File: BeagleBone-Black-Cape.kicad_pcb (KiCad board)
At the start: 2 copper layers, 54.6 x 86.9 mm, 48 parts, among them J1 MC000052, J10 MOLEX_2031, J11 MOLEX_2021, J12 EBV-02-D, J2 MOLEX_2051, J3 MOLEX_2031, J4 MOLEX_2021, J5 MOLEX_2041, J6 MOLEX_2031, J7 MOLEX_2041, J8 MOLEX_2031, J9 MOLEX_2041, P1 BeagleBone_Black_Header, P2 BeagleBone_Black_Header, Q1 IRLB8721PBF, Q2 IRFML8244, U1 DIGIPOT_50K, U2 U_IC-HKB, U3 X_STEPPER, U4 Y_STEPPER, U5 Z_STEPPER

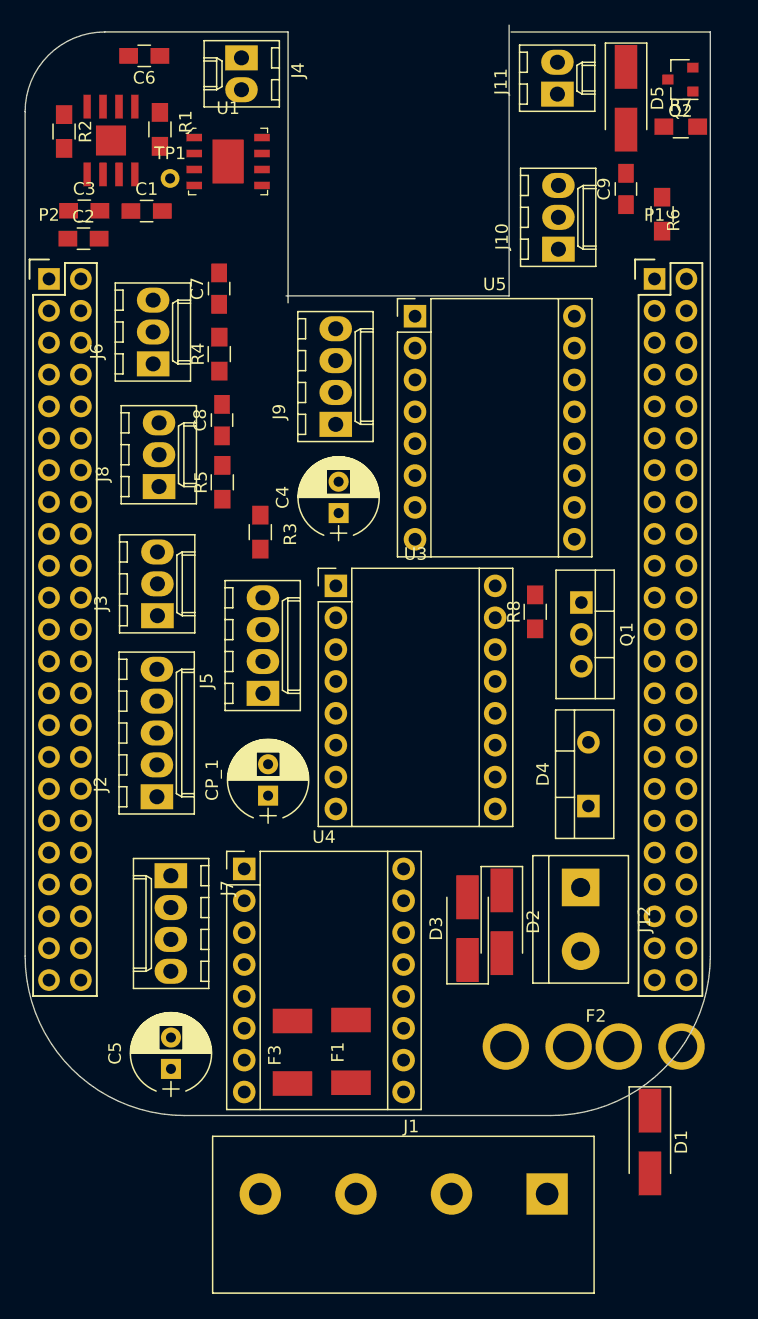
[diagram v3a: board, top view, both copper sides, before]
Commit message: moved power connector into direction of ethernet port idea is that board is placed on male headers to create more space
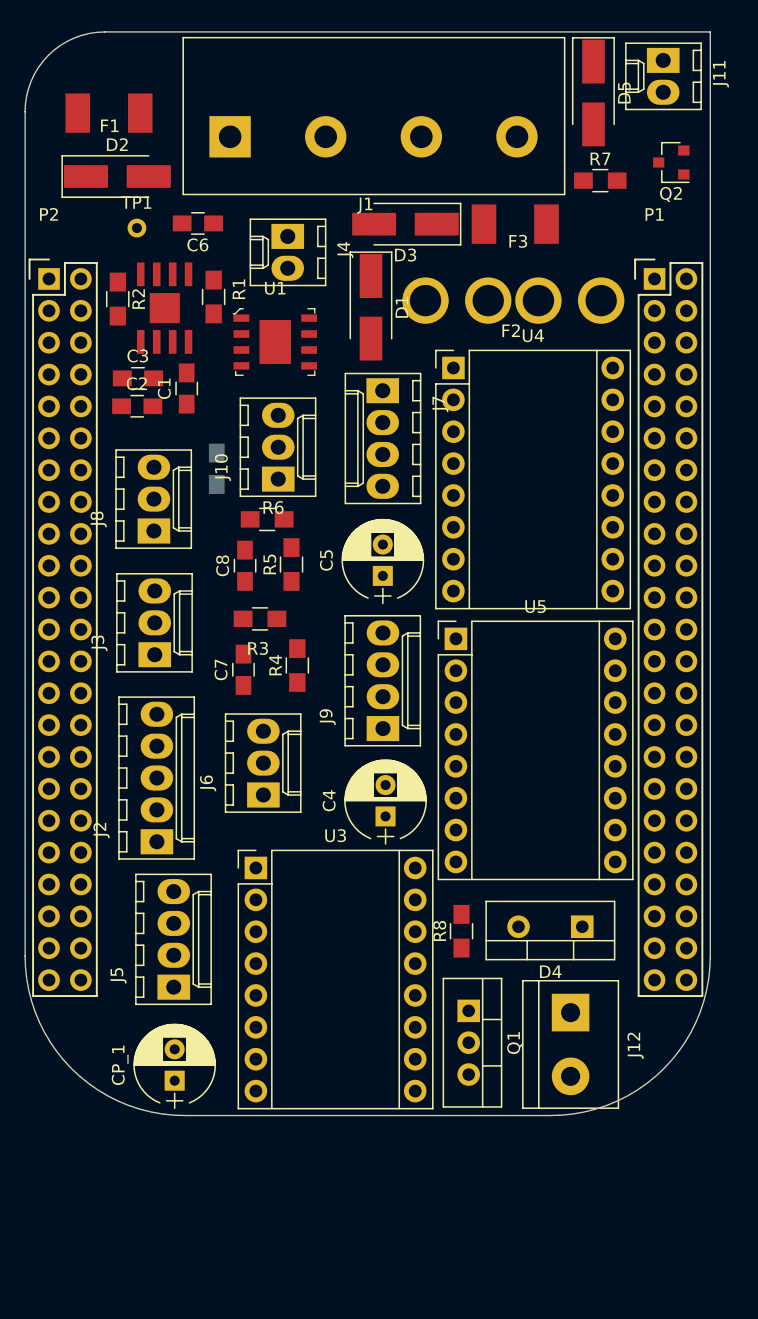
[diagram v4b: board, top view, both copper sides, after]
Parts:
- C9: moved to B.Cu
- moved J1 86.7 mm to (153.7, 51.1), turned to 180 degrees
- moved F1 77.3 mm to (121.2, 49.2), turned to 0 degrees
- moved D1 70.1 mm to (142.0, 64.6)
- moved F3 68.4 mm to (153.6, 58.0), turned to 0 degrees
- moved D2 66.8 mm to (121.8, 54.2), turned to 0 degrees
- moved F2 59.8 mm to (153.4, 64.1), turned to 180 degrees
- moved D3 56.4 mm to (144.8, 58.0), turned to 180 degrees
- moved U4 43.3 mm to (148.6, 69.5)
- moved C5 42.8 mm to (143.0, 86.1)
- moved J7 42.2 mm to (143.0, 71.3)
- moved R6 39.8 mm to (133.8, 81.5), turned to 180 degrees
- moved C9 39.5 mm to (129.7, 77.5), turned to 270 degrees
- moved J6 35.5 mm to (133.5, 103.5)
- moved Q1 33.8 mm to (149.8, 120.7)
- moved C7 30.4 mm to (131.9, 93.5)
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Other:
- board size 54.6 x 86.9 mm -> 54.6 x 86.4 mm

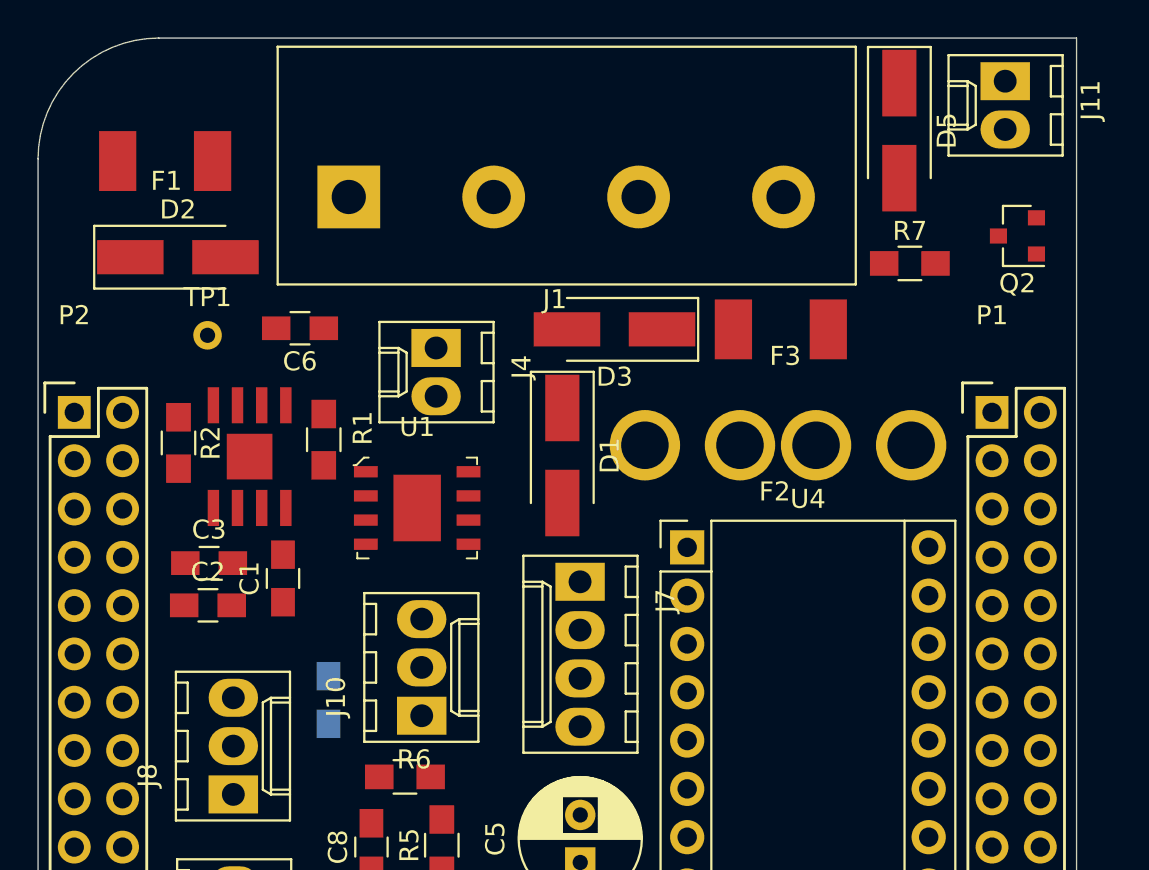
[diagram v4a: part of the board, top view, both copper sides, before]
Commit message: reorganized pcb and updated footprints
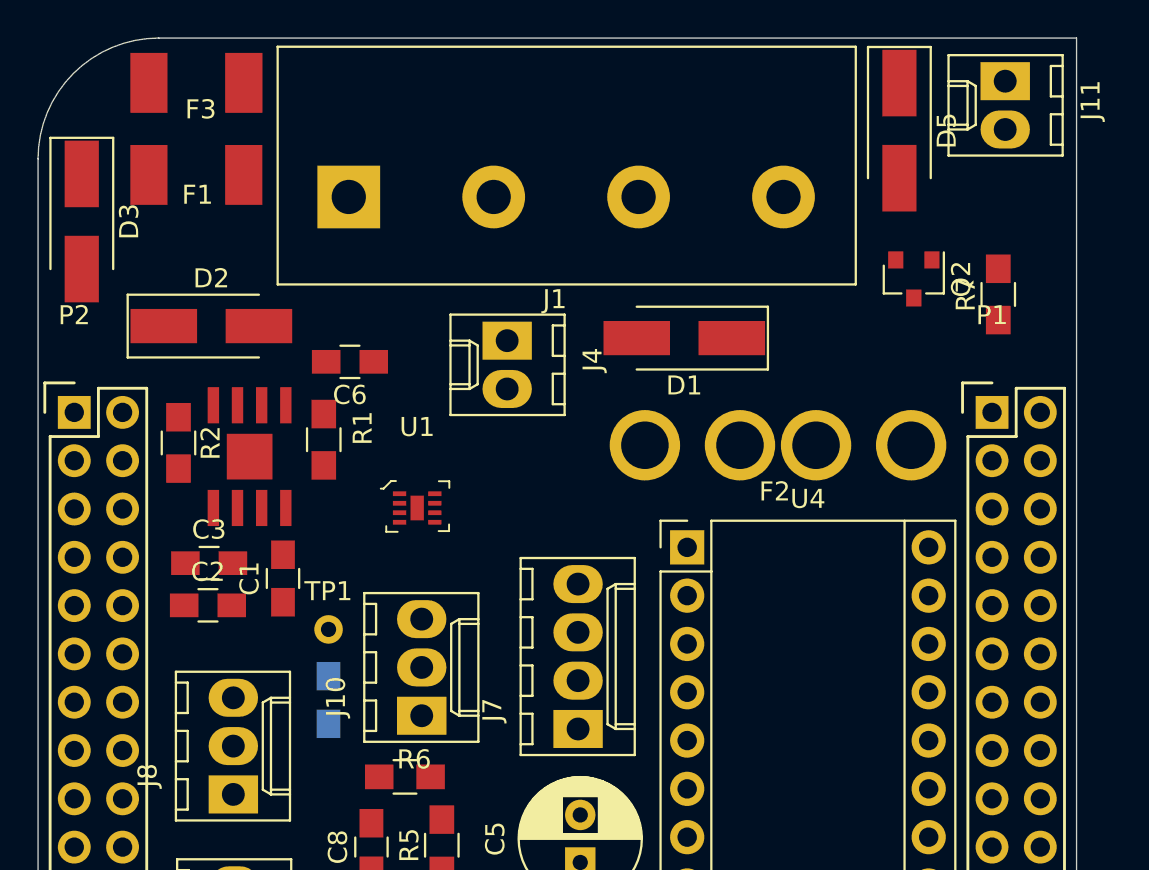
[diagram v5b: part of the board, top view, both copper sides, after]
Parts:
- moved F3 33.4 mm to (122.8, 45.1)
- moved D3 28.6 mm to (116.8, 52.3), turned to 270 degrees
- moved TP1 16.7 mm to (129.7, 73.8)
- moved D1 8.90 mm to (148.4, 58.5), turned to 180 degrees
- moved J7 7.74 mm to (142.9, 79.0), turned to 90 degrees
- moved Q2 5.90 mm to (160.5, 55.4), turned to 270 degrees
- moved R7 4.92 mm to (165.0, 56.2), turned to 90 degrees
- moved D2 4.03 mm to (123.6, 57.8)
- moved J4 3.76 mm to (139.1, 58.6)
- moved C6 3.17 mm to (130.9, 59.7)
- moved F1 1.80 mm to (122.8, 49.9)
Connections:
- D5 pad 1: +12V -> +24V
- J11 pad 1: +12V -> +24V
- J5 pad 1: X_1A -> X_2B
- J5 pad 2: X_1B -> X_2A
- J5 pad 3: X_2A -> X_1A
- J5 pad 4: X_2B -> X_1B
- J7 pad 1: Y_1A -> Y_2B
- J7 pad 2: Y_1B -> Y_2A
- J7 pad 3: Y_2A -> Y_1A
- J7 pad 4: Y_2B -> Y_1B
- J9 pad 1: Z_1A -> Z_2B
- J9 pad 2: Z_1B -> Z_2A
- J9 pad 3: Z_2A -> Z_1A
- J9 pad 4: Z_2B -> Z_1B
- P1 pad 13: SPINDLE_PWM -> FAN_PWM
- P1 pad 19: FAN_PWM -> SPINDLE_PWM

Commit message: started creating tracks
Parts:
- moved D3 5.95 mm to (122.0, 49.5), turned to 0 degrees
- moved R2 5.85 mm to (127.4, 65.8)
- moved U2 5.85 mm to (131.1, 66.6)
- moved R1 5.85 mm to (135.0, 65.7)
- moved U1 5.20 mm to (139.4, 66.0)
- moved F1 3.97 mm to (121.3, 53.6)
- moved C6 2.04 mm to (131.8, 57.9)
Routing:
- net GND: track 0.00 -> 168.2 mm
- net +24V: track 0.00 -> 98.4 mm
- net +12V: track 0.00 -> 37.3 mm
- net FAN_PWM: track 0.00 -> 30.1 mm
- net Net-(F2-Pad1): track 0.00 -> 29.6 mm
- net +5V: track 0.00 -> 26.6 mm
- net Net-(F3-Pad2): track 0.00 -> 23.2 mm
- net Net-(D5-Pad2): track 0.00 -> 12.0 mm
- net Net-(F1-Pad2): track 0.00 -> 8.62 mm

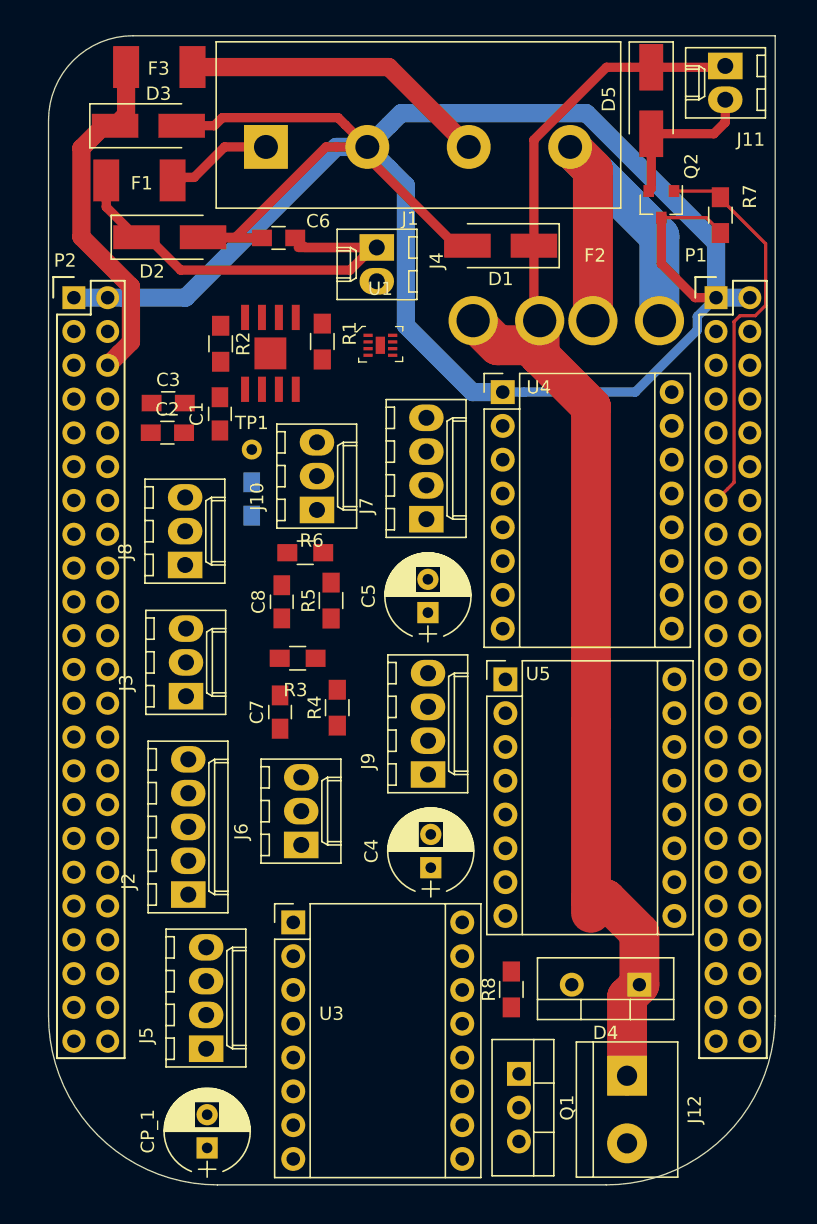
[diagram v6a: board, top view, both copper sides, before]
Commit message: added ground and power plane restored of 0, 5, 12, 24v connectors
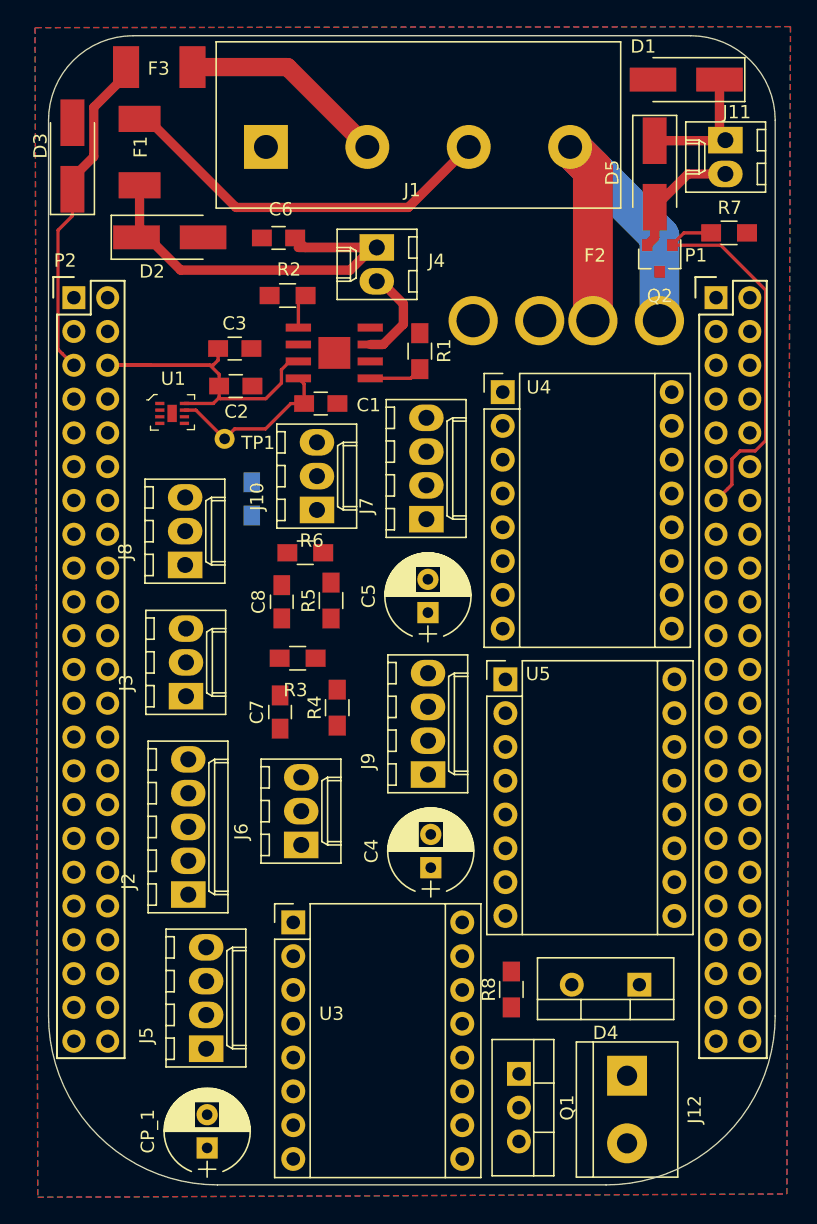
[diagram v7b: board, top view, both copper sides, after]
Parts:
- moved D1 18.7 mm to (162.4, 46.0)
- moved U1 16.5 mm to (123.8, 71.1)
- moved C1 7.62 mm to (134.9, 70.3), turned to 180 degrees
- moved R1 7.37 mm to (142.4, 66.4), turned to 90 degrees
- moved C3 6.46 mm to (128.5, 66.2), turned to 180 degrees
- moved C2 6.22 mm to (128.5, 69.0), turned to 180 degrees
- moved R2 6.20 mm to (132.4, 62.2), turned to 0 degrees
- moved D3 6.14 mm to (116.3, 51.7), turned to 90 degrees
- moved J11 5.58 mm to (165.3, 50.5)
- moved D5 5.53 mm to (160.0, 53.1)
- moved U2 4.80 mm to (135.9, 66.5), turned to 90 degrees
- moved Q2 4.07 mm to (160.4, 59.4)
- moved TP1 2.19 mm to (127.7, 73.0)
- moved F1 2.18 mm to (121.3, 51.4), turned to 90 degrees
- moved R7 1.48 mm to (165.6, 57.5), turned to 180 degrees
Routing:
- net GND: track 168.2 -> 0.57 mm
- net +24V: track 98.4 -> 10.1 mm
- net +5V: track 26.6 -> 58.6 mm
- net Net-(F1-Pad2): track 8.62 -> 29.4 mm
- net POT_W: track 0.00 -> 13.1 mm
- net Net-(F3-Pad2): track 23.2 -> 15.6 mm
- net LDK: track 0.00 -> 7.35 mm
- net IC_HB_PWM1: track 0.00 -> 4.01 mm
- net IC_HB_PWM2: track 0.00 -> 2.63 mm
- net Net-(D5-Pad2): track 12.0 -> 9.44 mm
- net +12V: track 37.3 -> 36.1 mm
- added copper zone on B.Cu, net +24V
- added copper zone on F.Cu, net GND
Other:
- outline, holes or cut-outs redrawn

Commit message: finished routing board....
still need to final check, add some text and make crucial tracks wider
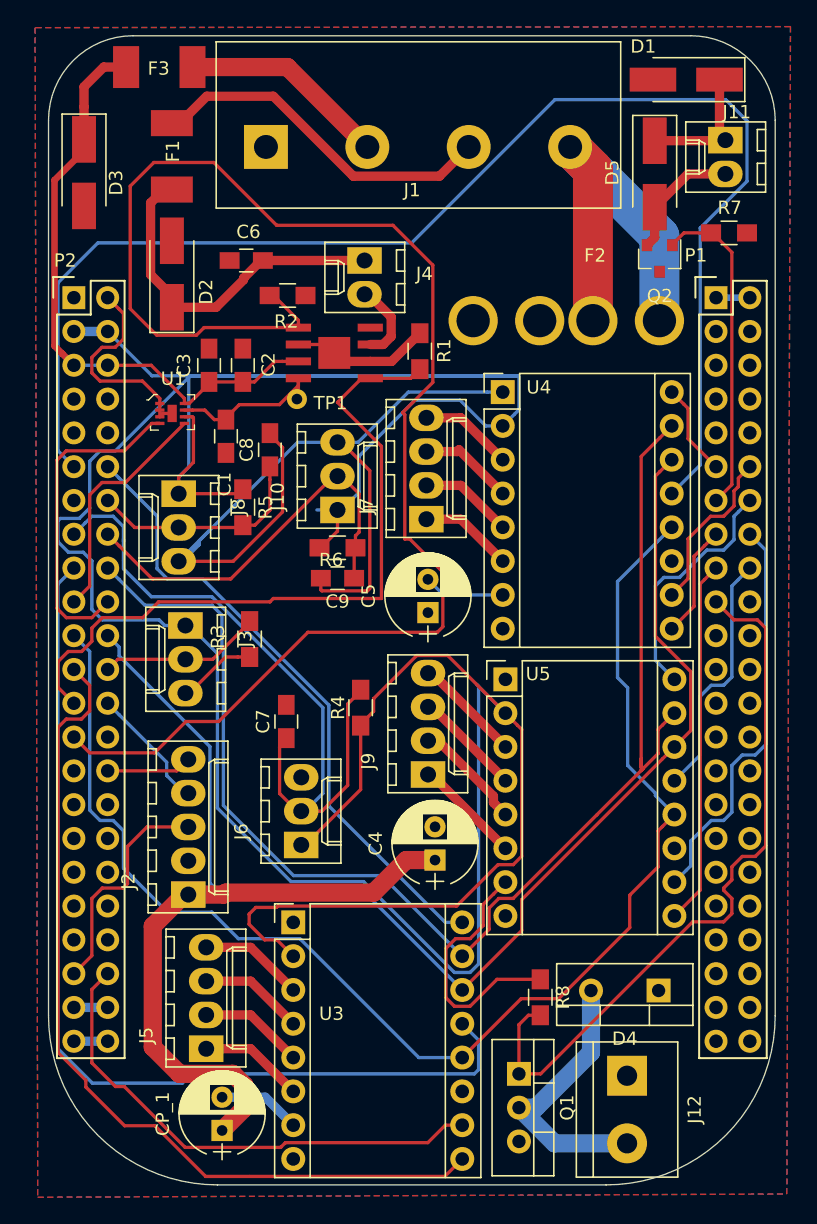
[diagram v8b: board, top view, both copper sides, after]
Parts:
- C9: moved to F.Cu
- moved C8 11.5 mm to (131.1, 73.8)
- moved R5 9.65 mm to (129.1, 78.1), turned to 270 degrees
- moved C9 8.78 mm to (136.2, 83.5), turned to 180 degrees
- moved C1 7.53 mm to (127.8, 72.8), turned to 90 degrees
- moved TP1 6.20 mm to (133.1, 70.0)
- moved J8 5.38 mm to (124.2, 77.1), turned to 270 degrees
- moved J3 5.31 mm to (124.8, 87.0), turned to 270 degrees
- moved R3 3.89 mm to (129.6, 88.0), turned to 90 degrees
- moved C6 2.96 mm to (129.3, 59.6)
- moved D2 2.77 mm to (123.7, 60.6), turned to 90 degrees
- moved R6 2.45 mm to (136.2, 81.2), turned to 0 degrees
- moved F1 2.45 mm to (123.7, 51.7)
- moved C3 2.30 mm to (126.5, 67.5), turned to 270 degrees
- moved R8 2.25 mm to (151.4, 115.0), turned to 270 degrees
- moved R4 1.76 mm to (137.9, 93.2)
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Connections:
- P1 pad 11: Y_DIR -> Y_ENABLE
- P1 pad 15: Z_DIR -> Y_DIR
- P1 pad 17: Y_ENABLE -> Z_DIR
- P1 pad 18: Z_PO -> SPIO_CSZ
- P2 pad 12: X_DIR -> X_ENABLE
- P2 pad 14: X_PO -> Y_PO
- P2 pad 15: X_ENABLE -> X_PO
- P2 pad 16: Y_PO -> Z_PO
- P2 pad 23: SPIO_CSZ -> X_DIR
- P2 pad 25: POLY_EN -> IC_HB_PWM1
- P2 pad 27: POLY_PWM -> IC_HB_PWM2
- P2 pad 30: IC_HB_PWM2 -> POLY_PWM
- P2 pad 41: IC_HB_PWM1 -> POLY_EN
- U3 pad 6: Net-(U3-Pad6) -> GND
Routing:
- net +3V3: track 0.00 -> 269.8 mm
- net GND: track 0.57 -> 139.0 mm
- net IC_HB_PWM2: track 2.63 -> 114.8 mm
- net SPIO_CSY: track 0.00 -> 102.8 mm
- net SPIO_DO: track 0.00 -> 102.5 mm
- net SPIO_DI: track 0.00 -> 100.2 mm
- net SPIO_SCL: track 0.00 -> 92.6 mm
- net SPI0_CSX: track 0.00 -> 74.1 mm
- net X_DIR: track 0.00 -> 66.0 mm
- net SPINDLE_PWM: track 0.00 -> 54.7 mm
- net X_PO: track 0.00 -> 54.4 mm
- net IC_HB_PWM1: track 4.01 -> 53.8 mm
- net X_ENABLE: track 0.00 -> 47.6 mm
- net +24V: track 10.1 -> 54.6 mm
- net X_STEP: track 0.00 -> 38.4 mm
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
